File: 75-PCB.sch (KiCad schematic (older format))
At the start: 303 parts, among them J1 AVR-ISP-6, SW1 SW_Push, U1 AT90USB1286-AU, U2 PRTR5V0U2X, Y1 16MHz

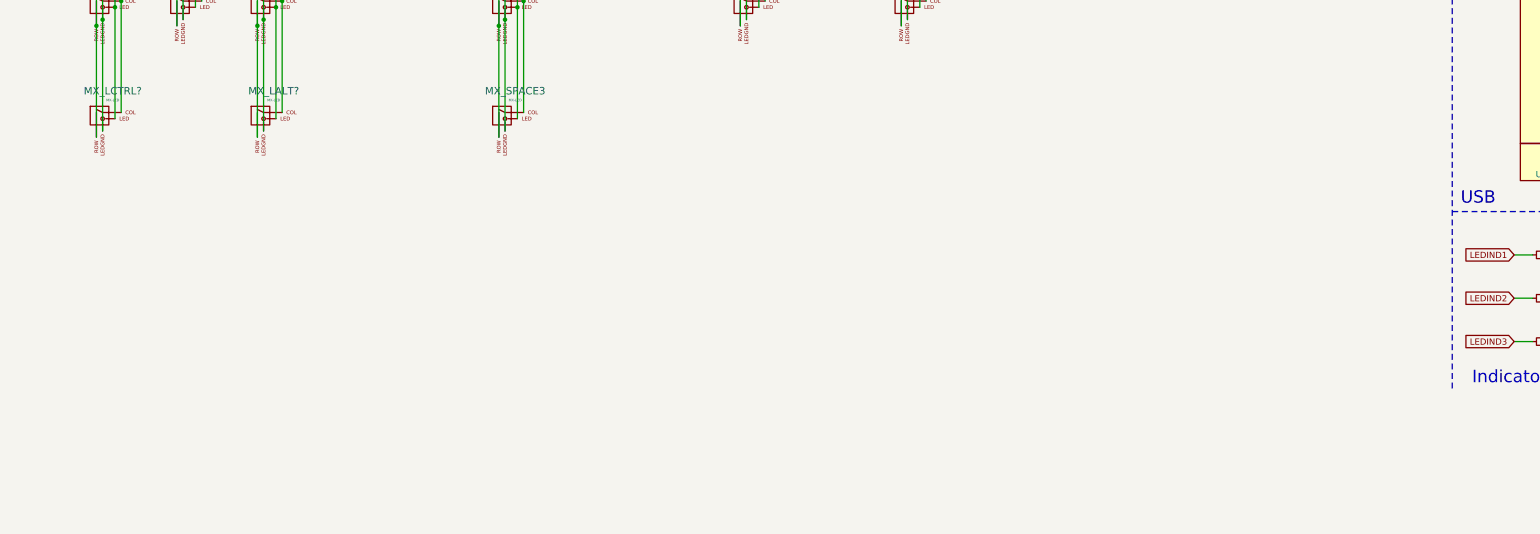
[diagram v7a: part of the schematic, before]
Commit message: Added Underglow LEDs
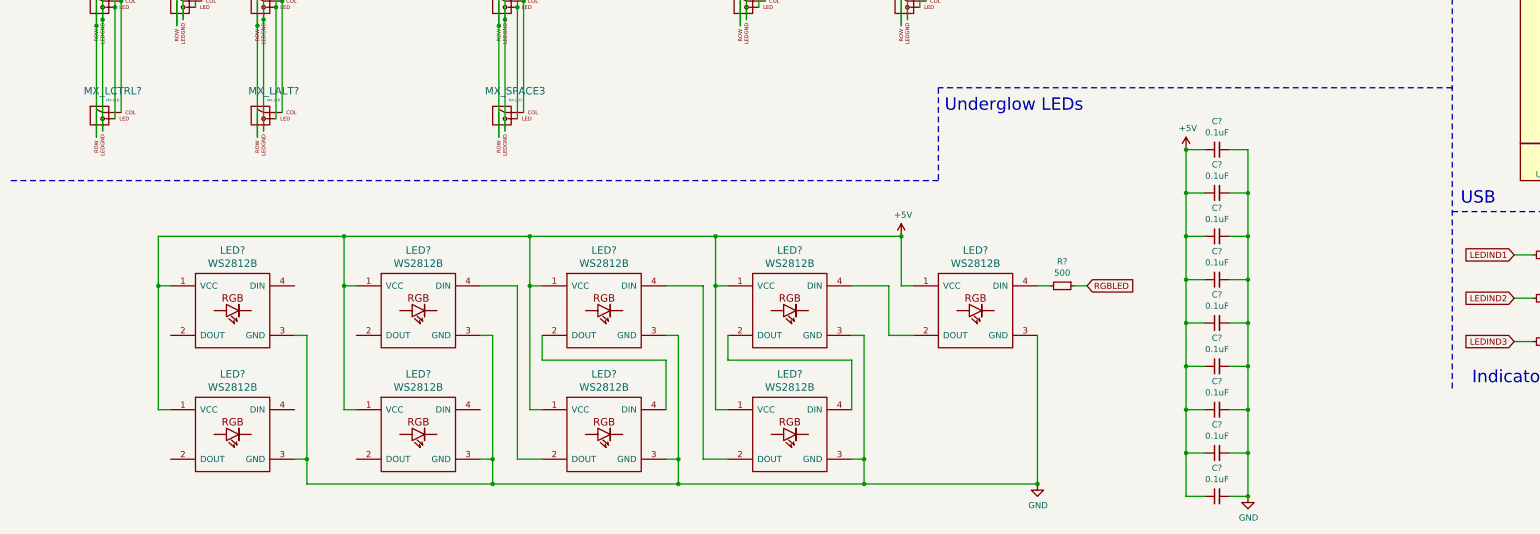
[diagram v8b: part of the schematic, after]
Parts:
- added C? (x9): 0.1uF, symbol Device:C_Small
- added LED? (x9): WS2812B, symbol ws2812b:WS2812B
- added R?: 500, symbol Device:R_Small
- J1: footprint (none) -> random-keyboard-parts:Reset_Pretty-Mask
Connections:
- net +5V: now also C?.1, C?.1, C?.1, C?.1, C?.1, C?.1, C?.1, C?.1, C?.1, LED?.1 (VCC), LED?.1 (VCC), LED?.1 (VCC), LED?.1 (VCC), LED?.1 (VCC), LED?.1 (VCC), LED?.1 (VCC), LED?.1 (VCC), LED?.1 (VCC)
- net GND: now also C?.2, C?.2, C?.2, C?.2, C?.2, C?.2, C?.2, C?.2, C?.2, LED?.3 (GND), LED?.3 (GND), LED?.3 (GND), LED?.3 (GND), LED?.3 (GND), LED?.3 (GND), LED?.3 (GND), LED?.3 (GND), LED?.3 (GND)
- new net: LED?.2 (DOUT), LED?.4 (DIN) (x5)
- new net: LED?.4 (DIN), R?.2
- new net RGBLED: R?.1
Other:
- note added: "Underglow LEDs"
